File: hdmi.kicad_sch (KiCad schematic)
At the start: 3 parts, among them U15 TPD4E05U06QDQARQ1, U17 TPD4E05U06QDQARQ1, U18 TPD4E05U06QDQARQ1

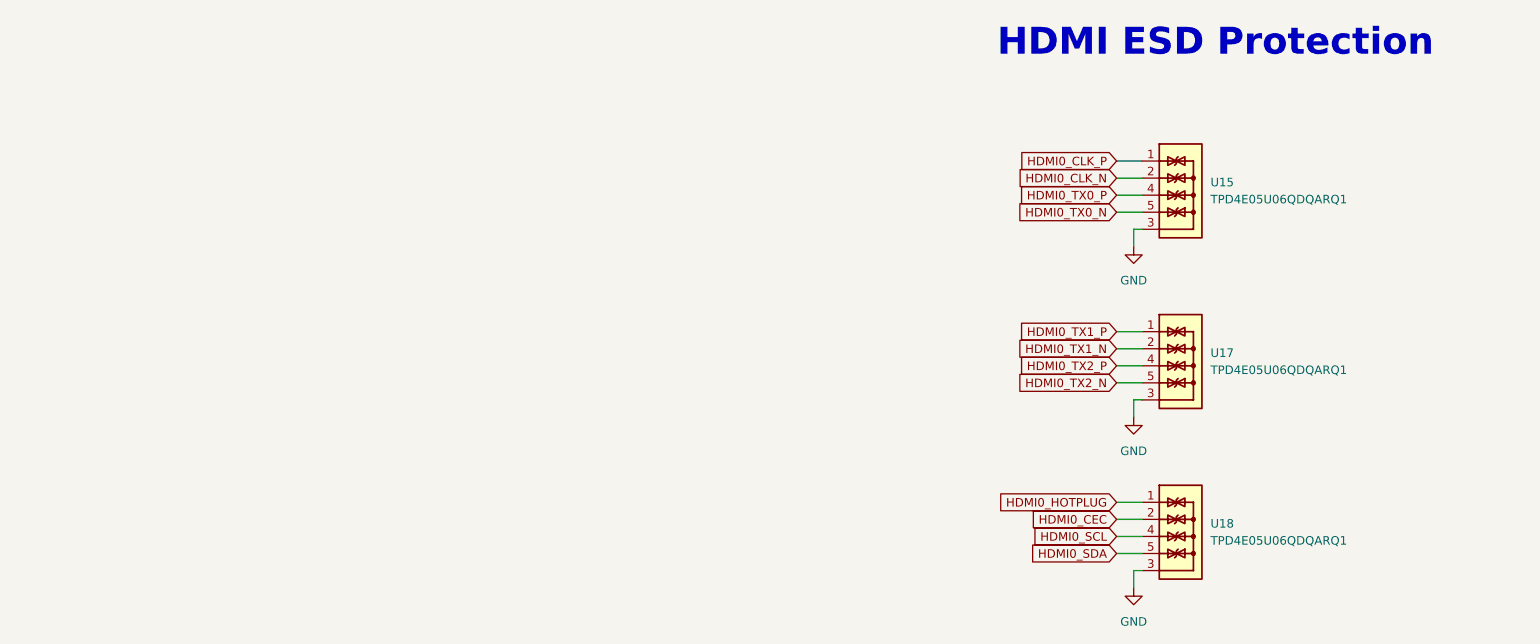
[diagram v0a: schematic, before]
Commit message: [#53847] Add SN75DP159RSBT to HDMI schematic
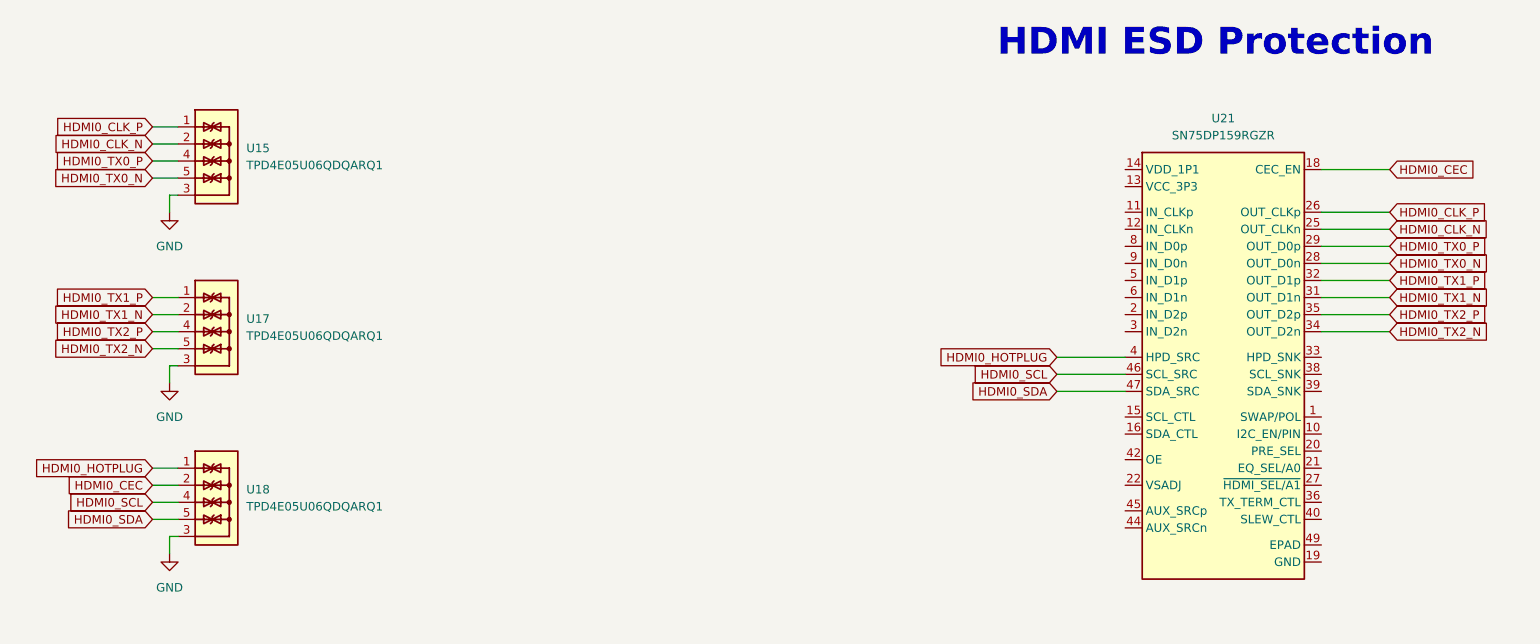
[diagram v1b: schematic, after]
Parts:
- added U21: SN75DP159_VQFN, antmicro-footprints:VQFN-48_7x7mm_P0.5mm_EP4.1x4.1mm, symbol antmicroInterfaceControllers:SN75DP159_VQFN
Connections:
- net HDMI0_CEC: now also U21.18 (CEC_EN)
- net HDMI0_CLK_N: now also U21.25 (OUT_CLKn)
- net HDMI0_CLK_P: now also U21.26 (OUT_CLKp)
- net HDMI0_HOTPLUG: now also U21.4 (HPD_SRC)
- net HDMI0_SCL: now also U21.46 (SCL_SRC)
- net HDMI0_SDA: now also U21.47 (SDA_SRC)
- net HDMI0_TX0_N: now also U21.28 (OUT_D0n)
- net HDMI0_TX0_P: now also U21.29 (OUT_D0p)
- net HDMI0_TX1_N: now also U21.31 (OUT_D1n)
- net HDMI0_TX1_P: now also U21.32 (OUT_D1p)
- net HDMI0_TX2_N: now also U21.34 (OUT_D2n)
- net HDMI0_TX2_P: now also U21.35 (OUT_D2p)
- new net: U21.13 (VCC_3P3), U21.43 (VCC_3P3)
- new net: U21.14 (VDD_1P1), U21.23 (VDD_1P1), U21.24 (VDD_1P1), U21.37 (VDD_1P1), U21.48 (VDD_1P1)
- new net: U21.19 (GND), U21.30 (GND), U21.41 (GND), U21.7 (GND)
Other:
- moved on the sheet: U15, U17, U18

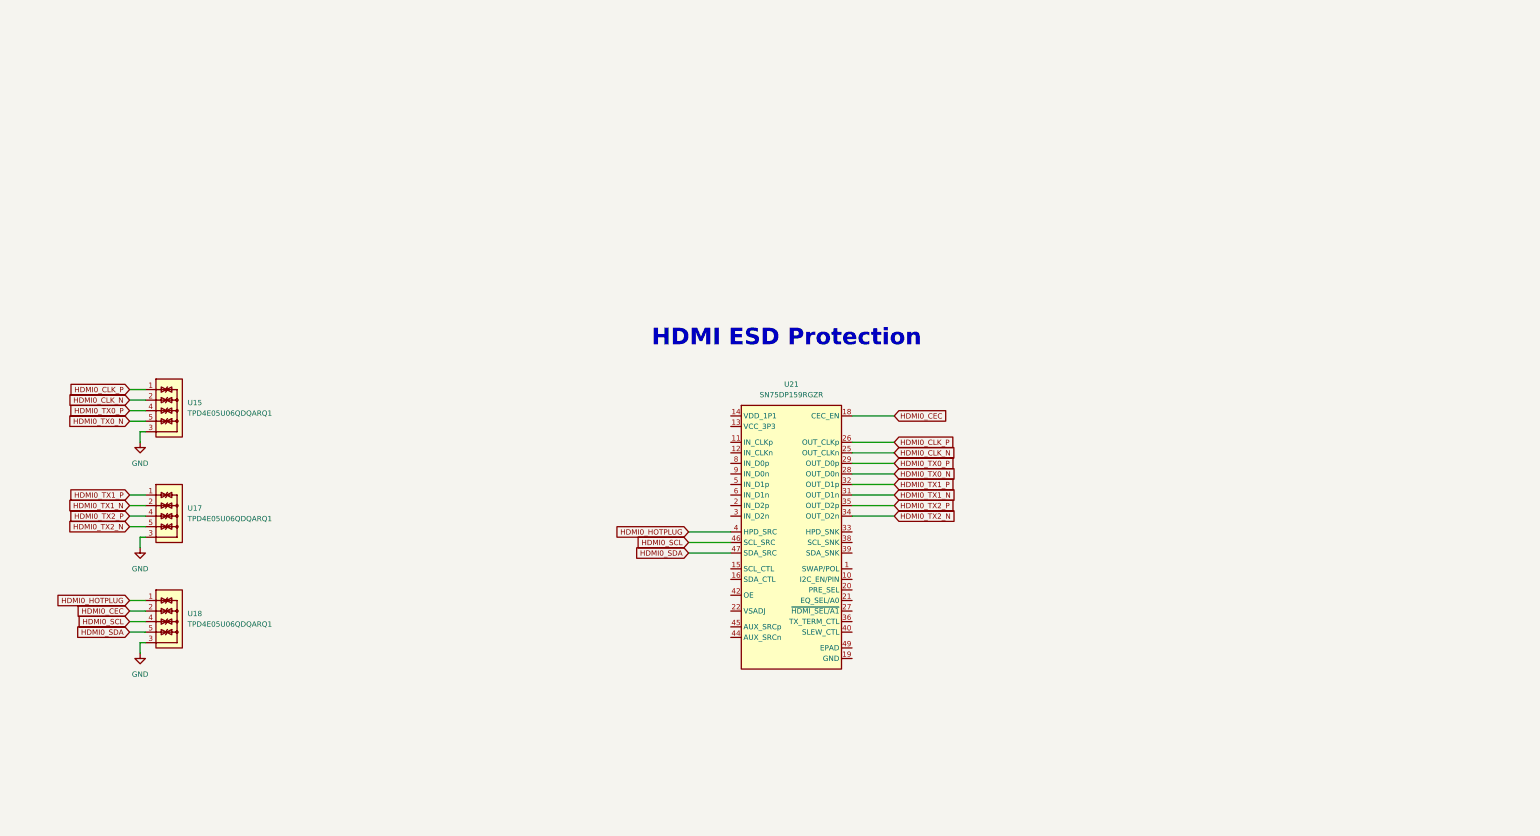
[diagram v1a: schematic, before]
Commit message: [#53847] Add HDMI
[#53847] Add HDMI driver power decoupling
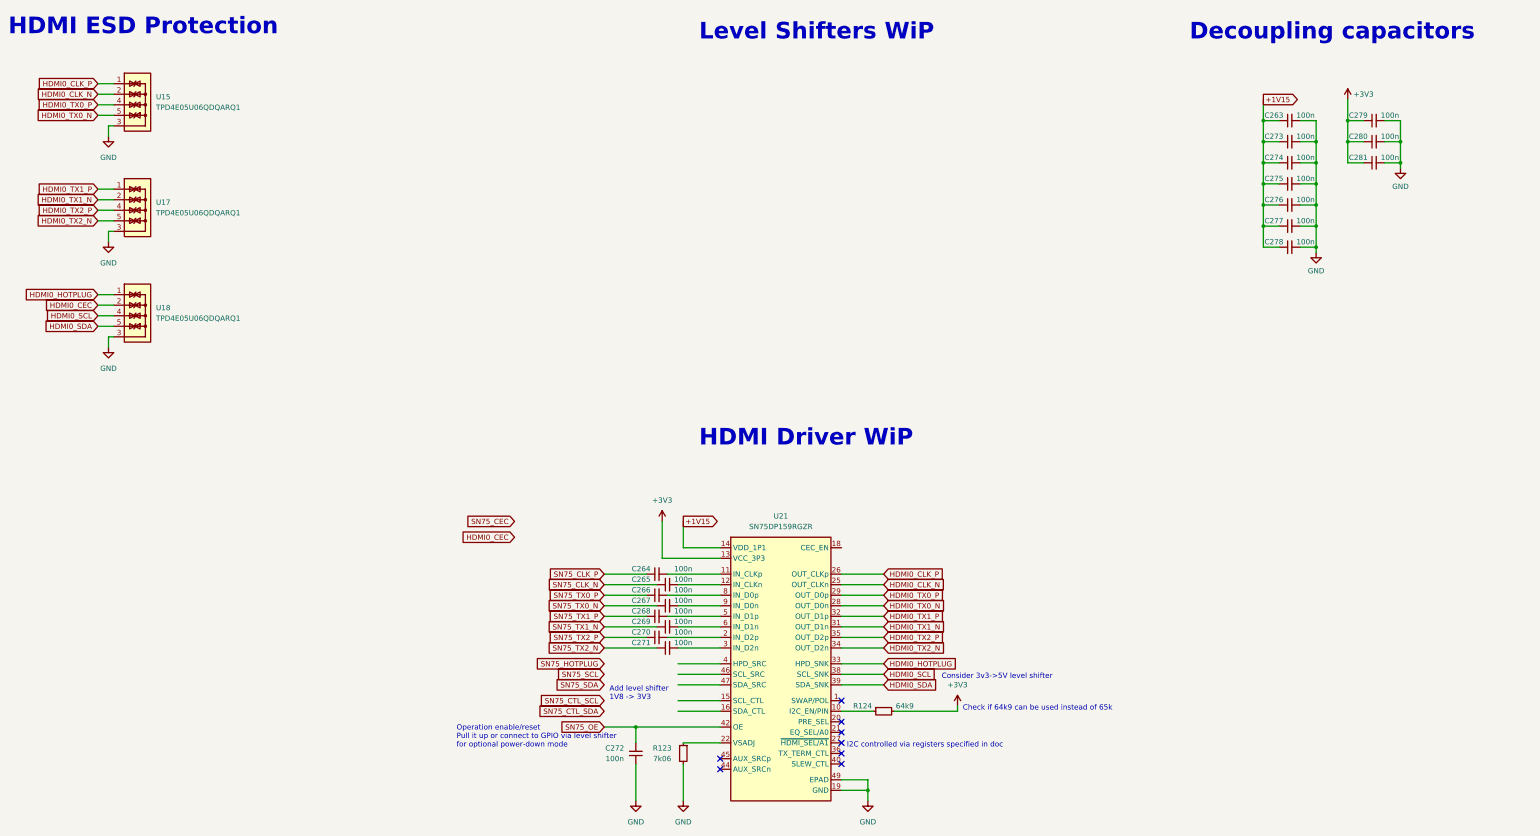
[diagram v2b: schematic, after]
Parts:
- added C263, C273, C274, C275, C276, C277, C278, C279, C280, C281: C_100n_0201_25V, antmicro-footprints:C_0201, symbol antmicroCapacitorsmisc:C_100n_0201_25V
- added C264, C265, C266, C267, C268, C269, C270, C271, C272: C_100n_0201, antmicro-footprints:C_0201, symbol antmicroCapacitorsmisc:C_100n_0201
- added R123: 7k06, antmicro-footprints:R_0402_1005Metric, symbol antmicroResistors0402:R_7k06_0402
- added R124: R_64k9_0402, antmicro-footprints:R_0402_1005Metric, symbol antmicroResistors0402:R_64k9_0402
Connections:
- net GND: now also U21.19 (GND), U21.30 (GND), U21.41 (GND), U21.49 (EPAD), U21.7 (GND), C263.2, C272.1, C273.2, C274.2, C275.2, C276.2, C277.2, C278.2, C279.2, C280.2, C281.2, R123.2
- net HDMI0_CEC: no longer U21.18 (CEC_EN)
- net HDMI0_HOTPLUG: now also U21.33 (HPD_SNK); no longer U21.4 (HPD_SRC)
- net HDMI0_SCL: now also U21.38 (SCL_SNK); no longer U21.46 (SCL_SRC)
- net HDMI0_SDA: now also U21.39 (SDA_SNK); no longer U21.47 (SDA_SRC)
- net at U21.10 (I2C_EN/PIN): now also R124.1
- net at U21.11 (IN_CLKp): now also C264.2
- net at U21.12 (IN_CLKn): now also C265.2
- net +3V3: now reaches U21.13 (VCC_3P3), U21.43 (VCC_3P3)
- net +3V3: now also C279.1, C280.1, C281.1, R124.2
- net +1V15: now reaches U21.14 (VDD_1P1), U21.23 (VDD_1P1), U21.24 (VDD_1P1), U21.37 (VDD_1P1), U21.48 (VDD_1P1)
- net +1V15: now also C263.1, C273.1, C274.1, C275.1, C276.1, C277.1, C278.1
- net at U21.2 (IN_D2p): now also C270.2
- net at U21.22 (VSADJ): now also R123.1
- net at U21.3 (IN_D2n): now also C271.2
- net SN75_OE: now reaches U21.42 (OE)
- net SN75_OE: now also C272.2
- net at U21.5 (IN_D1p): now also C268.2
- net at U21.6 (IN_D1n): now also C269.2
- net at U21.8 (IN_D0p): now also C266.2
- net at U21.9 (IN_D0n): now also C267.2
- new net SN75_CLK_N: C265.1
- new net SN75_CLK_P: C264.1
- new net SN75_TX0_N: C267.1
- new net SN75_TX0_P: C266.1
- new net SN75_TX1_N: C269.1
- new net SN75_TX1_P: C268.1
- new net SN75_TX2_N: C271.1
- new net SN75_TX2_P: C270.1
- no-connect marks 0 -> 8
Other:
- note added: "Add level shifter 1V8 -> 3V3"
- note added: "Check if 64k9 can be used instead of 65k"
- note added: "Consider 3v3->5V level shifter"
- note added: "Decoupling capacitors"
- note added: "HDMI Driver WiP"
- note added: "I2C controlled via registers specified in doc"
- note added: "Level Shifters WiP"
- note added: "Operation enable/reset Pull it up or connect to GPIO via level shifter for optional power-down mode"
- moved on the sheet: U15, U17, U18, U21

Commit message: [#53847] Add HDMI level shifters
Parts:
- removed C276, C277, C278, C279: C_100n_0201_25V, antmicro-footprints:C_0201, symbol antmicroCapacitorsmisc:C_100n_0201_25V
- added C276, C282: C_10n_0402, antmicro-footprints:C_0402_1005Metric, symbol antmicroCapacitors0402:C_10n_0402
- added C277, C278: C_10u_0402, antmicro-footprints:C_0402_1005Metric, symbol antmicroCapacitors0402:C_10u_0402
- added C284, C285, C286, C287, C288, C289: C_100n_0201_25V, antmicro-footprints:C_0201, symbol antmicroCapacitorsmisc:C_100n_0201_25V
- added Q3: NVJD4401NT1G, antmicro-footprints:SOT-363, symbol antmicroTransistorsFETsMOSFETsArrays:NVJD4401NT1G
- added R125, R126: R_4x2k2_0201_array, antmicro-footprints:R_Array_4x0201_Panasonic_EXB18V, symbol antmicroResistorNetworksArrays:R_4x2k2_0201_array
- added R127, R128: R_2k_0402, antmicro-footprints:R_0402_1005Metric, symbol antmicroResistors0402:R_2k_0402
- added R129: R_27k_0402, antmicro-footprints:R_0402_1005Metric, symbol antmicroResistors0402:R_27k_0402
- added R130, R134, R135, R137: R_10k_0402, antmicro-footprints:R_0402_1005Metric, symbol antmicroResistors0402:R_10k_0402
- added R131, R132: R_64k9_0402, antmicro-footprints:R_0402_1005Metric, symbol antmicroResistors0402:R_64k9_0402
- added R136: R_1k_0402, antmicro-footprints:R_0402_1005Metric, symbol antmicroResistors0402:R_1k_0402
- added U22: SN74AVC2T245_UQFN, antmicro-footprints:UQFN-10_1.4x1.8x0.5mm_P0.4mm, symbol antmicroLogicTranslatorsLevelShifters:SN74AVC2T245_UQFN
- added U23: NTS0104BQ, antmicro-footprints:DHVQFN-14-1EP_2.5x3mm, symbol antmicroLogicTranslatorsLevelShifters:NTS0104BQ
- added U24: SN74LVC1T45_SOT-5X3, antmicro-footprints:SOT-553-6, symbol antmicroLogicTranslatorsLevelShifters:SN74LVC1T45_SOT-5X3
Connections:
- net +1V15: now also C276.1, C277.1, C282.1
- net +3V3: now also C278.1, C285.2, C289.2, R126.5 (R4.2), R126.6 (R3.2), R126.7 (R2.2), R126.8 (R1.2), U22.6 (V_{CCB}), U23.14 (VCC_B)
- net GND: now also C276.2, C277.2, C278.2, C282.2, C284.1, C285.1, C286.1, C287.1, C288.1, C289.1, R131.2, R132.2, R136.1, R137.1, U22.3 (GND), U23.15 (GNDPAD), U23.7 (GND), U24.2 (GND)
- net HDMI0_CEC: now also Q3.4 (SOURCE2)
- net HDMI0_SCL: now also R128.1
- net HDMI0_SDA: now also R127.1
- net SN75_CEC: now also U24.4 (B)
- net SN75_CTL_SCL: now also R125.3 (R3.1), U23.4 (A3)
- net SN75_CTL_SDA: now also R125.4 (R4.1), U23.5 (A4)
- net SN75_HOTPLUG: now also U22.9 (A_{2})
- net SN75_OE: now also U22.8 (A_{1}); no longer C272.2, U21.42 (OE)
- net SN75_SCL: now also R125.1 (R1.1), U23.2 (A1)
- net SN75_SDA: now also R125.2 (R2.1), U23.3 (A2)
- net CTL_SCL: now reaches U21.15 (SCL_CTL)
- net CTL_SCL: now also R126.2 (R2.1), U23.11 (B3)
- net CTL_SDA: now reaches U21.16 (SDA_CTL)
- net CTL_SDA: now also R126.1 (R1.1), U23.10 (B4)
- net CEC_EN: now reaches U21.18 (CEC_EN)
- net CEC_EN: now also Q3.2 (GATE1), Q3.5 (GATE2)
- net at U21.21 (EQ_SEL/A0): now also R131.1
- net at U21.27 (~{HDMI_SEL/A1}): now also R132.1
- net HPD: now reaches U21.4 (HPD_SRC)
- net HPD: now also U22.4 (B_{2})
- net SCL: now reaches U21.46 (SCL_SRC)
- net SCL: now also R126.4 (R4.1), U23.13 (B1)
- net SDA: now reaches U21.47 (SDA_SRC)
- net SDA: now also R126.3 (R3.1), U23.12 (B2)
- new net: R130.1, U23.8 (OE)
- new net: R135.1, U22.10 (DIR_{1})
- new net: R134.1, U24.5 (DIR)
- new net: Q3.3 (DRAIN2), Q3.6 (DRAIN1)
- new net: R137.2, U22.1 (DIR_{2})
- new net: R136.2, U22.2 (~{OE})
- new net +5V: C287.2, R127.2, R128.2, R129.2, R134.2, U24.1 (VCCA)
- new net CEC: Q3.1 (SOURCE1), R129.1, U24.3 (A)
- new net OE: C272.2, U21.42 (OE), U22.5 (B_{1})
- new net VDDI: C284.2, C286.2, C288.2, R125.5 (R4.2), R125.6 (R3.2), R125.7 (R2.2), R125.8 (R1.2), R130.2, R135.2, U22.7 (V_{CCA}), U23.1 (VCC_A), U24.6 (VCCB)
- no-connect marks 8 -> 6
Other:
- note added: "CEC Enable"
- note added: "Change footprint to NTS0104UK - WLCSP12"
- note added: "Congif via I2C Regs specified in the doc"
- note added: "I2C_CTL address = BC/BD"
- note added: "Operation enable/reset"
- note added: "change footprint to SN74LVC1T45YZPR (DSBGA-6)"
- note removed: "Add level shifter 1V8 -> 3V3"
- note removed: "Check if 64k9 can be used instead of 65k"
- note removed: "Consider 3v3->5V level shifter"
- note removed: "I2C controlled via registers specified in doc"
- note removed: "Operation enable/reset Pull it up or connect to GPIO via level shifter for optional power-down mode"
- moved on the sheet: C263, C264, C265, C266, C267, C268, C269, C270, C271, C272, C273, C274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
